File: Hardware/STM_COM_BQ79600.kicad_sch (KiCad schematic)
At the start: 10 parts, among them U3 PBQ79600PWQ1

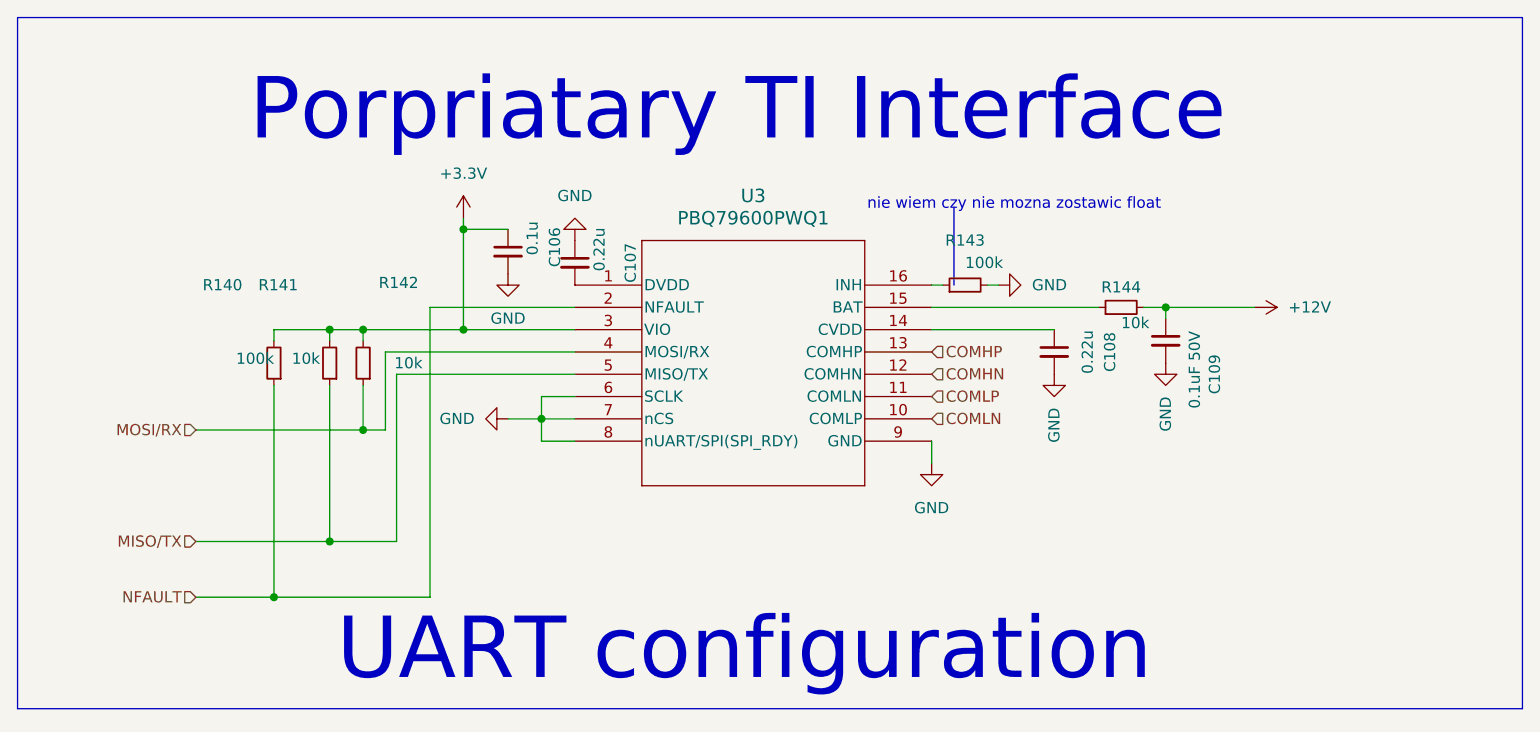
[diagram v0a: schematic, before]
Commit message: Dodano diody TVS na każdej części zasilania, zmieniono bezpieczniki, podzielono bezpieczniki na bezpieczniki do prądów wewnętrznych oraz zewnętrznych,poprawiono małe błedy
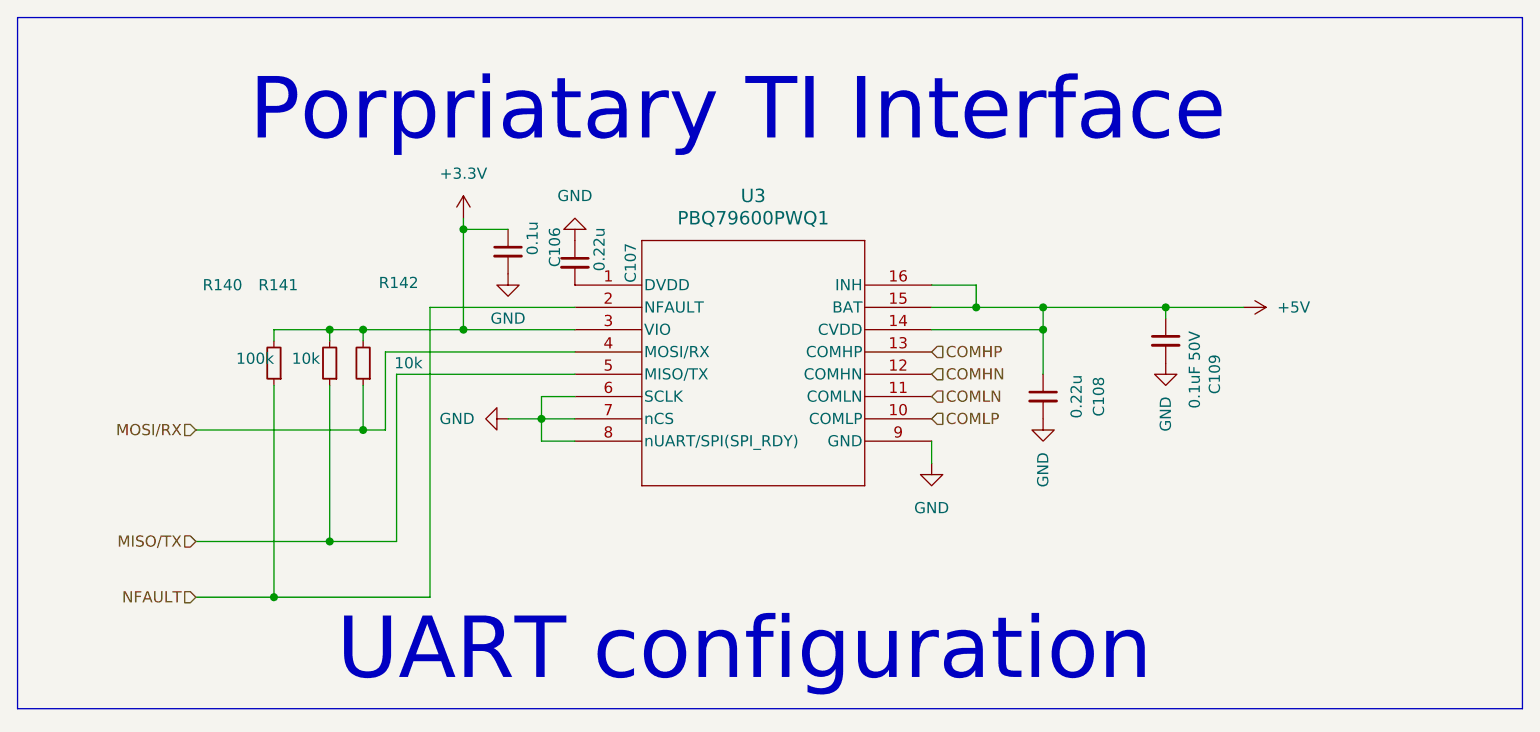
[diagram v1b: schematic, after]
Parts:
- removed R143: 100k, Resistor_SMD:R_0603_1608Metric_Pad0.98x0.95mm_HandSolder, symbol Device:R_Small
- removed R144: 10k, Resistor_SMD:R_0603_1608Metric_Pad0.98x0.95mm_HandSolder, symbol Device:R_Small
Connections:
- net +12V is gone; now on net +5V: C109.1
- net COMLN: now also U3.11 (COMLN); no longer U3.10 (COMLP)
- net COMLP: now also U3.10 (COMLP); no longer U3.11 (COMLN)
- net +5V: now reaches C108.1, U3.14 (CVDD)
- net +5V: now also U3.15 (BAT), U3.16 (INH)
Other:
- note removed: "nie wiem czy nie mozna zostawic float"
- moved on the sheet: C108

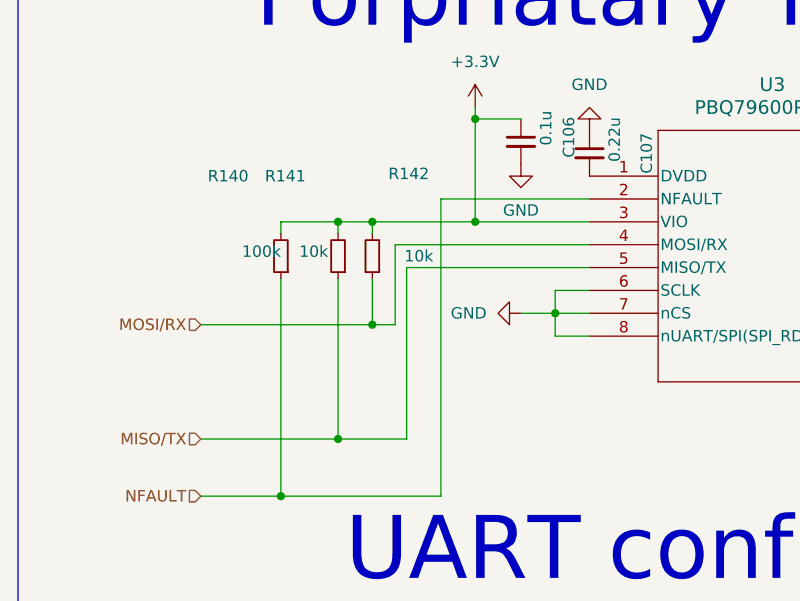
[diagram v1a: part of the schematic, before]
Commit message: Zmiany wizualne w schemacie
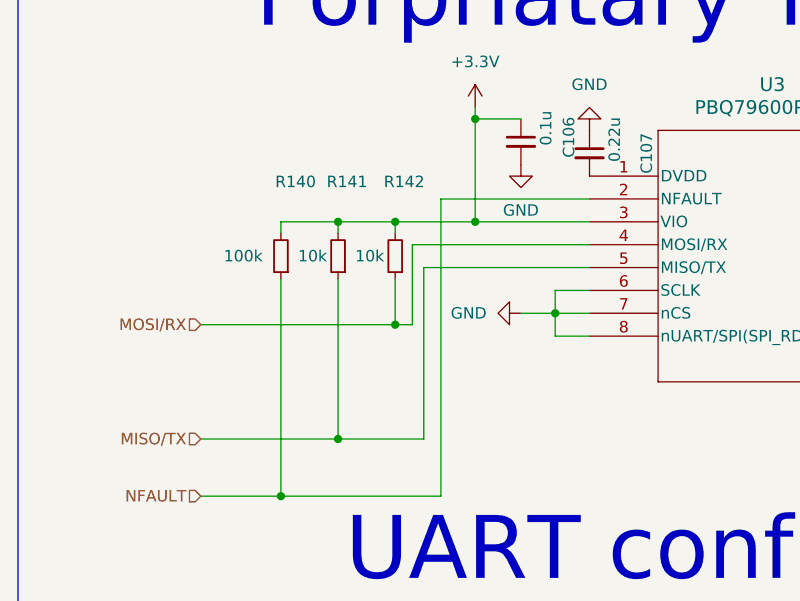
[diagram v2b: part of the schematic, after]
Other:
- moved on the sheet: R142
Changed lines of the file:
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@@
+	)
+	(junction
+		(at 95.25 92.71)
+		(diameter 0)
+		(color 0 0 0 0)
 	)
 	(junction
@@
 	)
 	(junction
-		(at 92.71 81.28)
+		(at 95.25 81.28)
 		(diameter 0)
 		(color 0 0 0 0)
@@
 		(color 0 0 0 0)
 	)
-	(junction
-		(at 92.71 92.71)
-		(diameter 0)
-		(color 0 0 0 0)
-	)
 	(wire
 		(pts
@@
 	(wire
 		(pts
-			(xy 92.71 87.63) (xy 92.71 92.71)
+			(xy 95.25 87.63) (xy 95.25 92.71)
 		)
 		(stroke
@@
 	(wire
 		(pts
-			(xy 95.25 83.82) (xy 95.25 92.71)
-		)
-		(stroke
-			(width 0)
-			(type default)
-		)
-	)
-	(wire
-		(pts
-			(xy 95.25 92.71) (xy 92.71 92.71)
-		)
-		(stroke
-			(width 0)
-			(type default)
-		)
-	)
-	(wire
-		(pts
-			(xy 73.66 92.71) (xy 92.71 92.71)
+			(xy 97.155 83.82) (xy 97.155 92.71)
+		)
+		(stroke
+			(width 0)
+			(type default)
+		)
+	)
+	(wire
+		(pts
+			(xy 97.155 92.71) (xy 95.25 92.71)
+		)
+		(stroke
+			(width 0)
+			(type default)
+		)
+	)
+	(wire
+		(pts
+			(xy 73.66 92.71) (xy 95.25 92.71)
 		)
 		(stroke
@@
 	(wire
 		(pts
-			(xy 96.52 86.36) (xy 96.52 105.41)
+			(xy 98.425 86.36) (xy 98.425 105.41)
 		)
 		(stroke
@@
 	(wire
 		(pts
-			(xy 88.9 105.41) (xy 96.52 105.41)
+			(xy 88.9 105.41) (xy 98.425 105.41)
 		)
 		(stroke
@@
 	(wire
 		(pts
-			(xy 92.71 82.55) (xy 92.71 81.28)
+			(xy 95.25 82.55) (xy 95.25 81.28)
 		)
 		(stroke
@@
 	(wire
 		(pts
-			(xy 92.71 81.28) (xy 104.14 81.28)
-		)
-		(stroke
-			(width 0)
-			(type default)
-		)
-	)
-	(wire
-		(pts
 			(xy 88.9 105.41) (xy 73.66 105.41)
 		)
@@
 	(wire
 		(pts
-			(xy 116.84 86.36) (xy 96.52 86.36)
+			(xy 116.84 86.36) (xy 98.425 86.36)
 		)
 		(stroke
@@
 	(wire
 		(pts
-			(xy 116.84 83.82) (xy 95.25 83.82)
+			(xy 116.84 83.82) (xy 97.155 83.82)
 		)
 		(stroke
@@
 	(wire
 		(pts
-			(xy 88.9 81.28) (xy 92.71 81.28)
+			(xy 88.9 81.28) (xy 95.25 81.28)
 		)
 		(stroke
@@
 		(pts
 			(xy 104.14 69.85) (xy 109.22 69.85)
+		)
+		(stroke
+			(width 0)
+			(type default)
+		)
+	)
+	(wire
+		(pts
+			(xy 95.25 81.28) (xy 104.14 81.28)
 		)
 		(stroke
@@
 	(symbol
 		(lib_id "Device:R_Small")
-		(at 92.71 85.09 180)
+		(at 95.25 85.09 180)
 		(unit 1)
 		(exclude_from_sim no)
@@
 		(dnp no)
 		(property "Reference" "R142"
-			(at 94.488 75.946 0)
+			(at 93.98 76.835 0)
 			(effects
 				(font
@@
 		)
 		(property "Value" "10k"
-			(at 96.266 85.09 0)
+			(at 90.805 85.09 0)
 			(effects
 				(font
@@
 		)
 		(property "Footprint" "Resistor_SMD:R_0603_1608Metric_Pad0.98x0.95mm_HandSolder"
-			(at 92.71 85.09 0)
+			(at 95.25 85.09 0)
 			(effects
 				(font
@@
 		)
 		(property "Datasheet" "https://www.mouser.pl/ProductDetail/Vishay-Dale/CRCW060310K0FKEI?qs=sGAEpiMZZMvdGkrng054t8tsKUCh5%2FbYoR58PzIQdJA%3D"
-			(at 92.71 85.09 0)
+			(at 95.25 85.09 0)
 			(effects
 				(font
@@
 		)
 		(property "Description" "Resistor, small symbol"
-			(at 92.71 85.09 0)
+			(at 95.25 85.09 0)
 			(effects
 				(font
@@
 		(dnp no)
 		(property "Reference" "R141"
-			(at 80.772 76.2 0)
+			(at 87.63 76.835 0)
 			(effects
 				(font
@@
 		)
 		(property "Value" "10k"
-			(at 84.582 84.582 0)
+			(at 84.455 85.09 0)
 			(effects
 				(font
@@
 		(dnp no)
 		(property "Reference" "R140"
-			(at 74.422 76.2 0)
+			(at 81.915 76.835 0)
 			(effects
 				(font
@@
 		)
 		(property "Value" "100k"
-			(at 78.232 84.582 0)
-			(effects
-				(font
+			(at 76.2 85.09 0)
+			(effects
+				(font
